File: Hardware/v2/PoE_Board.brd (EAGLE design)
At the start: 84.6 x 72.1 mm, 93 parts, among them U1 EDISON_CONNECTOR_FULLMOUNTING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, U2 LAN9512-JZX, U3 MAX4995AAUT+, U4 EDISON_CONNECTOR_FULLHEADER

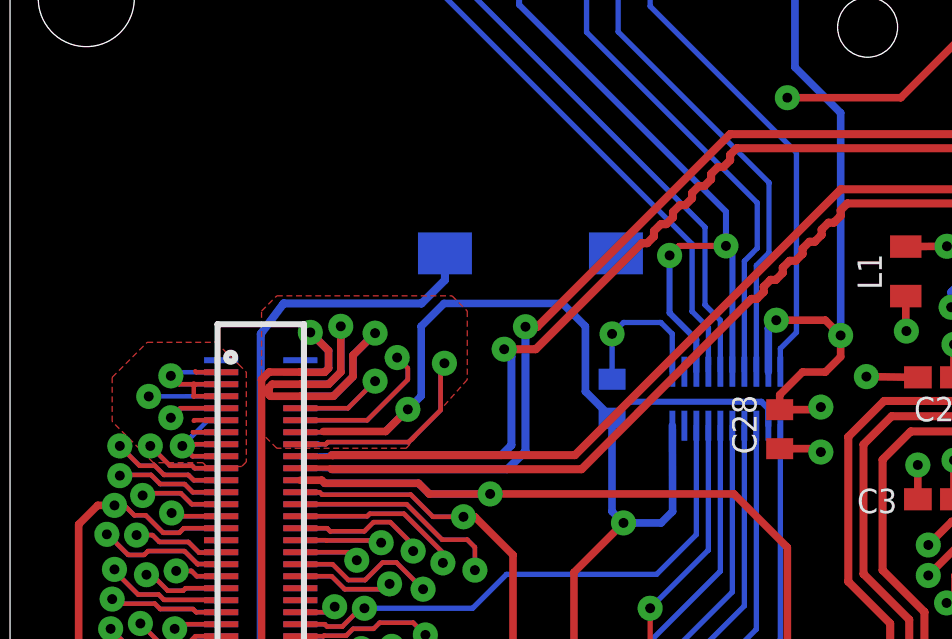
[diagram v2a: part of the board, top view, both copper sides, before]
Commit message: Connected shield pins on Ethernet jack
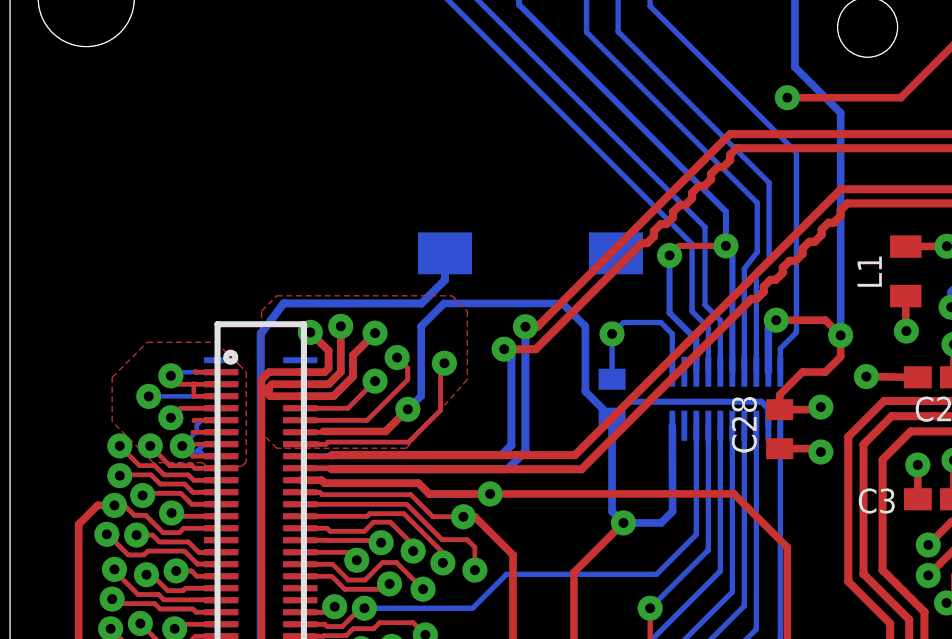
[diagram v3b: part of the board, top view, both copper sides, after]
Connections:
- net SHLD: now also X1.S1, X1.S2
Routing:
- net GND: track 147.3 -> 146.3 mm
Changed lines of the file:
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@@
 <grid distance="5" unitdist="mil" unit="mil" style="lines" multiple="1" display="yes" altdistance="0.25" altunitdist="mil" altunit="mil"/>
 <layers>
-<layer number="1" name="Top" color="4" fill="1" visible="no" active="yes"/>
+<layer number="1" name="Top" color="4" fill="1" visible="yes" active="yes"/>
 <layer number="2" name="gnd" color="11" fill="3" visible="yes" active="yes"/>
 <layer number="3" name="pwr" color="13" fill="3" visible="yes" active="yes"/>
@@
 <contactref element="U4" pad="13"/>
 <contactref element="U4" pad="15"/>
-<wire x1="5.7666" y1="49.1928" x2="5.327" y2="49.1928" width="0.1524" layer="16"/>
-<wire x1="5.327" y1="49.1928" x2="4.4704" y2="48.3362" width="0.1524" layer="16"/>
-<wire x1="5.7666" y1="48.7928" x2="4.927" y2="48.7928" width="0.1524" layer="16"/>
-<wire x1="4.927" y1="48.7928" x2="4.4704" y2="48.3362" width="0.1524" layer="16"/>
-<wire x1="5.7666" y1="48.3928" x2="4.527" y2="48.3928" width="0.1524" layer="16"/>
-<wire x1="4.527" y1="48.3928" x2="4.4704" y2="48.3362" width="0.1524" layer="16"/>
-<wire x1="5.7666" y1="47.9928" x2="4.8138" y2="47.9928" width="0.1524" layer="16"/>
-<wire x1="4.8138" y1="47.9928" x2="4.4704" y2="48.3362" width="0.1524" layer="16"/>
 <contactref element="U4" pad="5"/>
 <wire x1="5.7666" y1="49.9928" x2="3.3528" y2="49.9872" width="0.1524" layer="16"/>
+<wire x1="5.7666" y1="49.1928" x2="5.1238" y2="49.1928" width="0.1524" layer="16"/>
+<wire x1="5.1238" y1="49.1928" x2="4.953" y2="49.022" width="0.1524" layer="16"/>
+<wire x1="4.953" y1="49.022" x2="4.953" y2="48.8188" width="0.1524" layer="16"/>
+<wire x1="4.953" y1="48.8188" x2="4.4704" y2="48.3362" width="0.1524" layer="16"/>
+<wire x1="5.7666" y1="48.7928" x2="4.979" y2="48.7928" width="0.1524" layer="16"/>
+<wire x1="4.979" y1="48.7928" x2="4.953" y2="48.8188" width="0.1524" layer="16"/>
+<wire x1="5.7666" y1="48.3928" x2="5.2001" y2="48.3928" width="0.1524" layer="16"/>
+<wire x1="5.2001" y1="48.3928" x2="5.01015" y2="48.20285" width="0.1524" layer="16"/>
+<wire x1="5.01015" y1="48.20285" x2="4.95935" y2="48.15205" width="0.1524" layer="16"/>
+<wire x1="4.95935" y1="48.15205" x2="4.65455" y2="48.15205" width="0.1524" layer="16"/>
+<wire x1="4.65455" y1="48.15205" x2="4.4704" y2="48.3362" width="0.1524" layer="16"/>
+<wire x1="5.7666" y1="47.9928" x2="5.2202" y2="47.9928" width="0.1524" layer="16"/>
+<wire x1="5.2202" y1="47.9928" x2="5.01015" y2="48.20285" width="0.1524" layer="16"/>
 </signal>
 <signal name="N$1">
@@
 </polygon>
 <contactref element="R10" pad="1"/>
+<contactref element="X1" pad="S1"/>
+<contactref element="X1" pad="S2"/>
 </signal>
 <signal name="USBSHLD">
@@
 <contactref element="USD" pad="2"/>
 <contactref element="U6" pad="18"/>
-<wire x1="23.606" y1="50.811" x2="23.606" y2="54.3527" width="0.1778" layer="16"/>
-<wire x1="23.606" y1="54.3527" x2="24.0284" y2="54.7751" width="0.1778" layer="16"/>
-<wire x1="24.0284" y1="54.7751" x2="24.0284" y2="57.1119" width="0.1778" layer="16"/>
+<wire x1="23.606" y1="50.811" x2="23.606" y2="54.0987" width="0.1778" layer="16"/>
+<wire x1="23.606" y1="54.0987" x2="24.0284" y2="54.5211" width="0.1778" layer="16"/>
+<wire x1="24.0284" y1="54.5211" x2="24.0284" y2="57.1119" width="0.1778" layer="16"/>
 <wire x1="24.0284" y1="57.1119" x2="18.9992" y2="62.1411" width="0.1778" layer="16"/>
 <wire x1="18.9992" y1="62.1411" x2="18.9992" y2="64.436" width="0.1778" layer="16"/>
@@
 <contactref element="USD" pad="3"/>
 <contactref element="U6" pad="17"/>
-<wire x1="23.206" y1="50.811" x2="23.206" y2="54.4957" width="0.1778" layer="16"/>
-<wire x1="23.206" y1="54.4957" x2="23.6347" y2="54.9275" width="0.1778" layer="16"/>
-<wire x1="23.6347" y1="54.9275" x2="23.6347" y2="56.4388" width="0.1778" layer="16"/>
+<wire x1="23.206" y1="50.811" x2="23.206" y2="54.2417" width="0.1778" layer="16"/>
+<wire x1="23.206" y1="54.2417" x2="23.6347" y2="54.8005" width="0.1778" layer="16"/>
+<wire x1="23.6347" y1="54.8005" x2="23.6347" y2="56.4388" width="0.1778" layer="16"/>
 <wire x1="23.6347" y1="56.4388" x2="17.9451" y2="62.1284" width="0.1778" layer="16"/>
 <wire x1="17.9451" y1="62.1284" x2="17.9451" y2="64.7827" width="0.1778" layer="16"/>

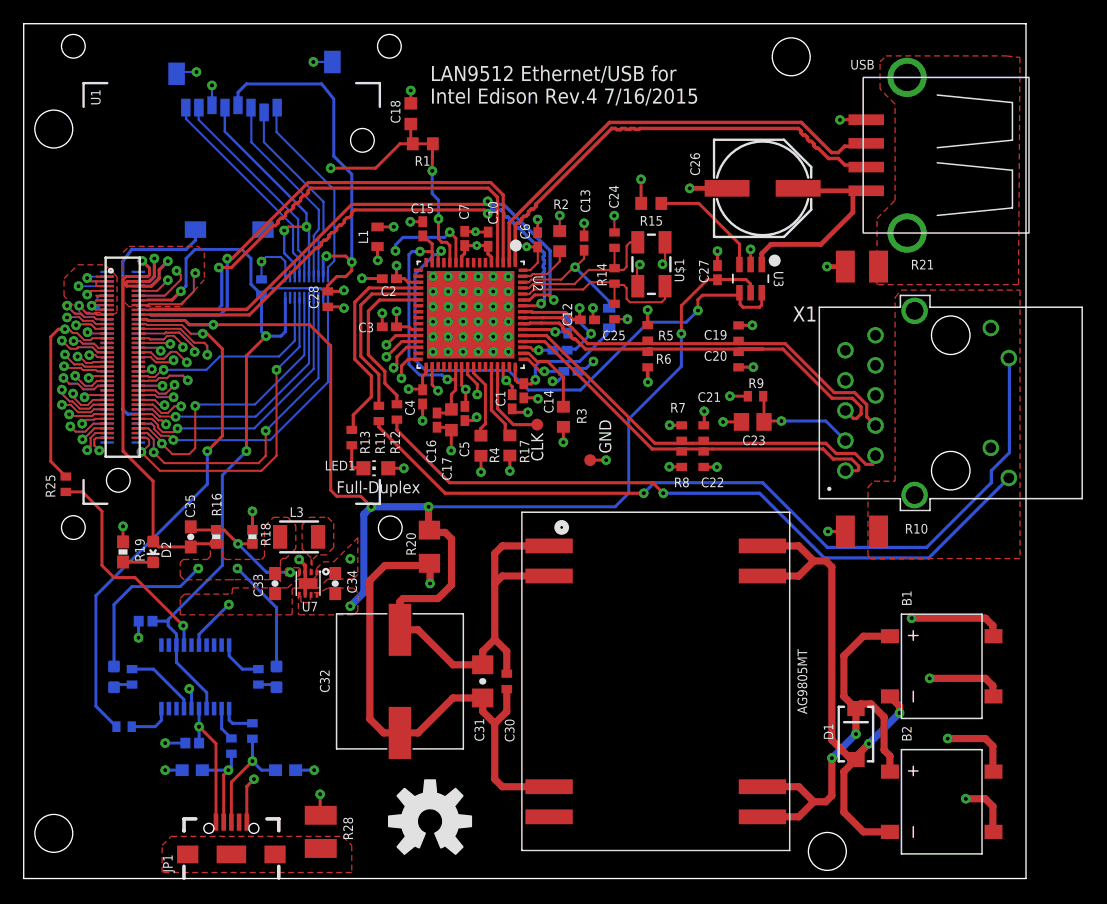
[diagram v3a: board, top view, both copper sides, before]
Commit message: Moved U8 to top of board, moved LED1 from under the Edison, put C28 back on the bottom
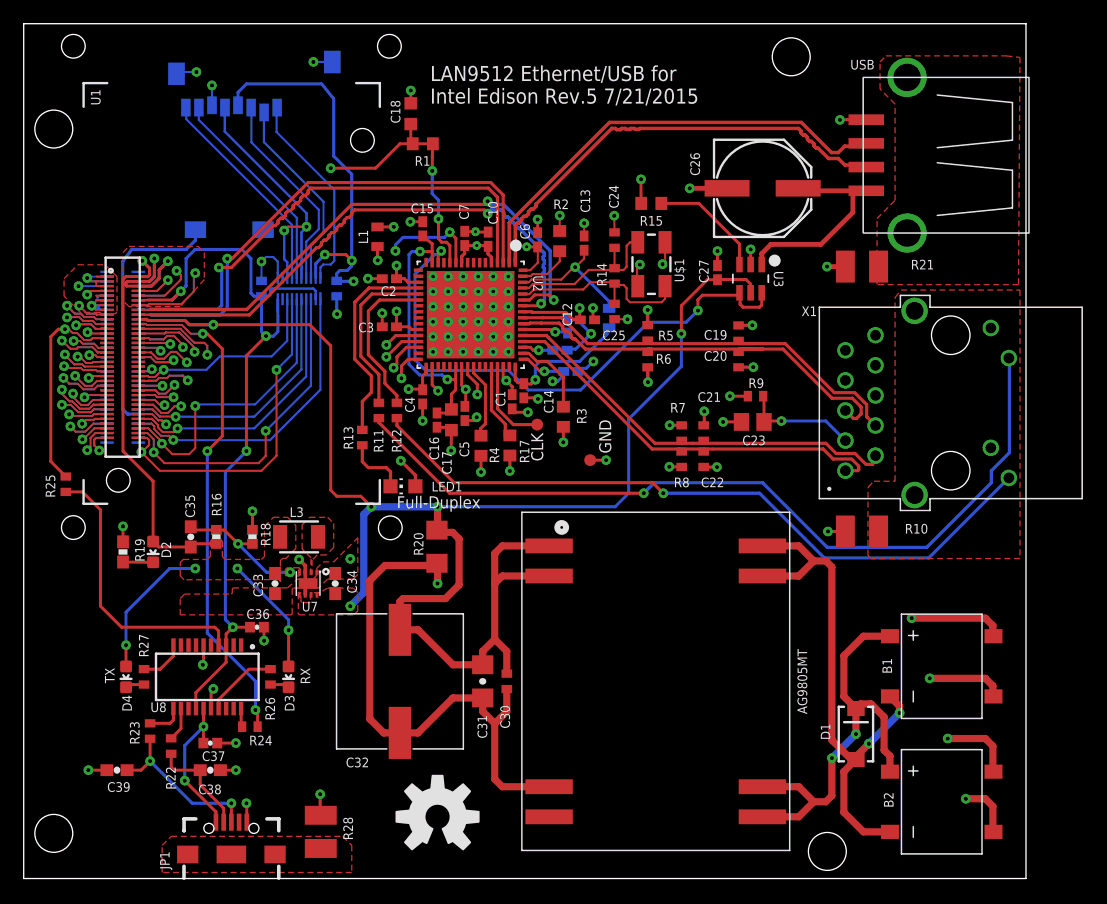
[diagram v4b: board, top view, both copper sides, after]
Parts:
- moved D3 14.7 mm to (21.1, 17.0), flipped to the top
- moved C39 14.2 mm to (6.60, 9.14), flipped to the top
- moved D4 12.7 mm to (7.37, 17.0), flipped to the top
- moved R26 11.7 mm to (19.6, 17.0), flipped to the top
- moved R24 10.6 mm to (17.8, 12.8), flipped to the top
- moved R27 9.65 mm to (8.89, 17.0), flipped to the top
- moved C36 9.41 mm to (18.4, 21.2), flipped to the top
- moved R23 8.64 mm to (9.40, 12.4), flipped to the top
- moved R22 5.08 mm to (11.2, 11.2), flipped to the top
- moved LED1 2.75 mm to (30.7, 33.1)
- moved C37 1.52 mm to (14.5, 11.4), flipped to the top
- moved C38 1.52 mm to (14.5, 9.14), flipped to the top
- moved C28 1.17 mm to (25.1, 49.8), flipped to the bottom
- moved U8 1.02 mm to (14.2, 17.0), flipped to the top
- moved R13 0.89 mm to (27.3, 37.2)
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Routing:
- net GND: track 146.3 -> 139.2 mm
- net S$22: track 18.9 -> 23.7 mm, vias 1 -> 0
- net S$17: track 10.0 -> 14.1 mm, vias 1 -> 2
- net P22: track 50.8 -> 47.9 mm, vias 2 -> 3
- net N$19: track 2.82 -> 5.34 mm
- net 2_VCCA_1V8: track 72.2 -> 69.9 mm, vias 3 -> 4
- net S$23: track 3.71 -> 1.56 mm
- net VDD3IO: track 147.6 -> 149.0 mm
- net VSYS: track 87.9 -> 86.7 mm, vias 6 -> 8
- net VBUS1: track 12.0 -> 13.2 mm, vias 1 -> 2
- net 8_A7_SDCLKFB: track 20.8 -> 20.1 mm
- net 20_B1_NC: track 16.5 -> 17.3 mm
- net S$15: track 8.24 -> 8.89 mm, vias 1 -> 0
- net S$5: track 44.2 -> 44.8 mm
- net USB_VBUS: track 144.0 -> 144.6 mm
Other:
- board text added: "LAN9512 Ethernet/USB for Intel Edison Rev.5 7/21/2015"
- board text removed: "LAN9512 Ethernet/USB for Intel Edison Rev.4 7/16/2015"

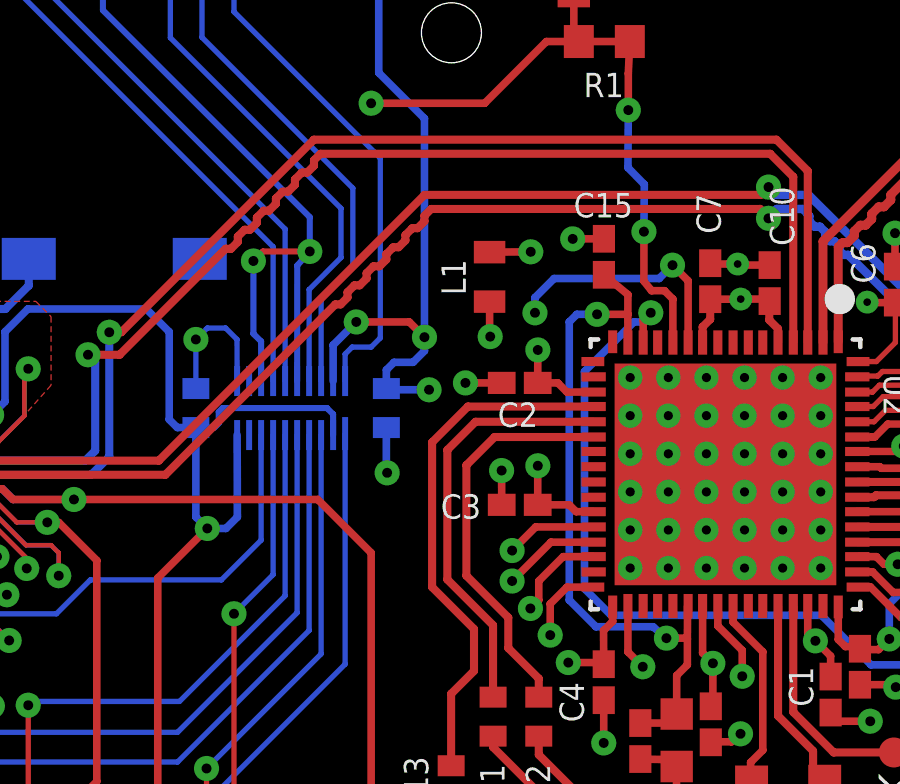
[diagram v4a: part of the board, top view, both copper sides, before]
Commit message: Minor changes in via placement
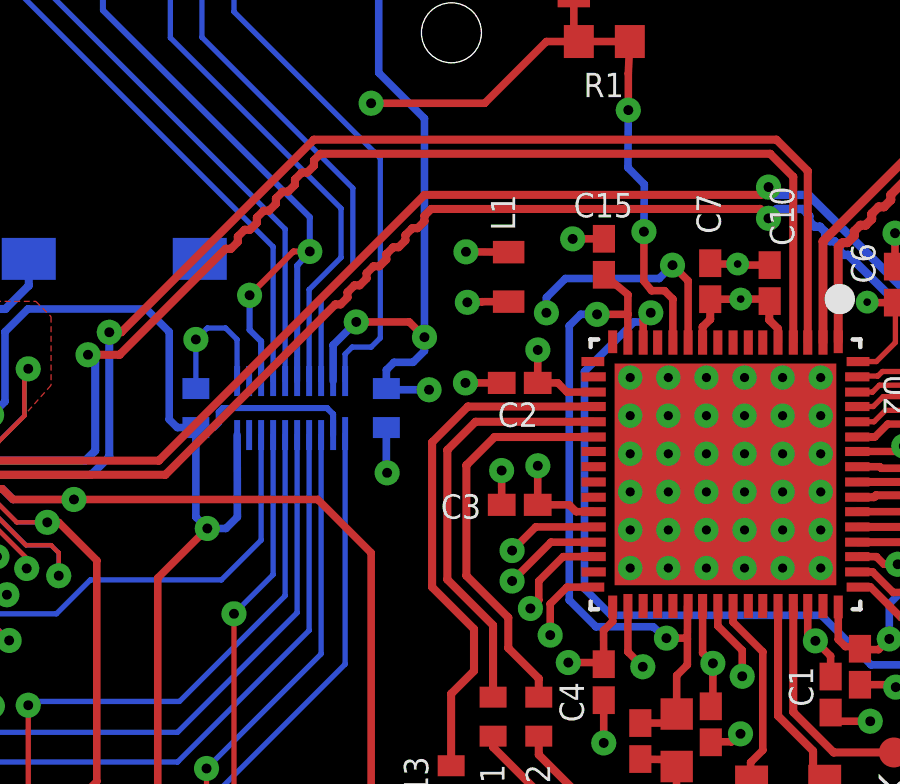
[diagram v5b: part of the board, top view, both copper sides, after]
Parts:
- moved L1 0.64 mm to (29.2, 54.2)
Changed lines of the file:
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@@
 <attribute name="NAME" x="70.541" y="69.0848" size="0.8128" layer="25" ratio="15" rot="R180"/>
 </element>
-<element name="L1" library="murata-inductors" package="L0603" value="2.0A 120Ohm" x="28.587" y="54.1562" smashed="yes" rot="R90">
-<attribute name="NAME" x="27.792" y="53.5442" size="0.8128" layer="25" ratio="15" rot="R90"/>
+<element name="L1" library="murata-inductors" package="L0603" value="2.0A 120Ohm" x="29.222" y="54.1562" smashed="yes" rot="R90">
+<attribute name="NAME" x="29.443" y="55.7032" size="0.8128" layer="25" ratio="15" rot="R90"/>
 </element>
 <element name="L2" library="murata-inductors" package="L0603" value="2.0A 120Ohm" x="48.133" y="47.2948" smashed="yes" rot="MR270">
@@
 <via x="42.1894" y="44.577" extent="1-16" drill="0.3302"/>
 <wire x1="40.844" y1="44.8302" x2="40.8432" y2="44.831" width="0.1524" layer="1"/>
-<wire x1="28.587" y1="54.9812" x2="29.9586" y2="54.9918" width="0.254" layer="1"/>
-<via x="29.9586" y="54.9918" extent="1-16" drill="0.3302"/>
+<wire x1="29.222" y1="54.9812" x2="27.7996" y2="54.9918" width="0.254" layer="1"/>
+<via x="27.7996" y="54.9918" extent="1-16" drill="0.3302"/>
 <via x="42.672" y="42.799" extent="1-16" drill="0.3302"/>
 <wire x1="40.894" y1="43.7642" x2="40.8686" y2="43.815" width="0.1524" layer="1"/>
@@
 <wire x1="33.195259375" y1="52.9082" x2="32.1691" y2="52.9082" width="0.254" layer="1"/>
 <via x="32.1691" y="52.9082" extent="1-16" drill="0.3302"/>
-<wire x1="32.1691" y1="52.9082" x2="31.496" y2="52.9082" width="0.254" layer="16"/>
-<wire x1="31.496" y1="52.9082" x2="31.242" y2="52.6542" width="0.254" layer="16"/>
-<wire x1="31.242" y1="52.6542" x2="31.242" y2="43.3832" width="0.254" layer="16"/>
+<wire x1="32.1691" y1="52.9082" x2="31.623" y2="52.9082" width="0.254" layer="16"/>
+<wire x1="31.623" y1="52.9082" x2="31.242" y2="52.5272" width="0.254" layer="16"/>
+<wire x1="31.242" y1="52.5272" x2="31.242" y2="43.3832" width="0.254" layer="16"/>
 <wire x1="31.242" y1="43.3832" x2="32.131" y2="42.4942" width="0.254" layer="16"/>
 <wire x1="32.131" y1="42.4942" x2="34.036" y2="42.4942" width="0.254" layer="16"/>
@@
 <wire x1="15.6972" y1="65.0372" x2="15.716" y2="65.056" width="0.2032" layer="16"/>
 <wire x1="20.971" y1="50.684" x2="20.971" y2="52.0065" width="0.2032" layer="16"/>
-<wire x1="20.971" y1="52.0065" x2="20.7137" y2="52.2605" width="0.2032" layer="16"/>
-<wire x1="20.7137" y1="52.2605" x2="20.7137" y2="54.6862" width="0.2032" layer="16"/>
-<wire x1="20.7137" y1="54.6862" x2="21.0312" y2="55.0037" width="0.2032" layer="1"/>
-<via x="20.7137" y="54.6862" extent="1-16" drill="0.3302"/>
+<wire x1="20.971" y1="52.0065" x2="20.5867" y2="52.3875" width="0.2032" layer="16"/>
+<wire x1="20.5867" y1="52.3875" x2="20.5867" y2="53.5432" width="0.2032" layer="16"/>
+<wire x1="20.5867" y1="53.5432" x2="22.0472" y2="55.0037" width="0.2032" layer="1"/>
+<via x="20.5867" y="53.5432" extent="1-16" drill="0.3302"/>
 <via x="22.5933" y="55.0037" extent="1-16" drill="0.3302"/>
-<wire x1="21.0312" y1="55.0037" x2="22.5933" y2="55.0037" width="0.2032" layer="1"/>
+<wire x1="22.0472" y1="55.0037" x2="22.5933" y2="55.0037" width="0.2032" layer="1"/>
 <wire x1="22.5933" y1="56.1467" x2="22.5933" y2="55.0037" width="0.2032" layer="16"/>
 </signal>
@@
 <wire x1="30.191" y1="50.6222" x2="30.191" y2="50.81595" width="0.254" layer="1"/>
 <wire x1="30.861" y1="50.6222" x2="30.191" y2="50.6222" width="0.254" layer="1"/>
-<via x="30.099" y="52.959" extent="1-16" drill="0.3302"/>
+<via x="30.48" y="52.959" extent="1-16" drill="0.3302"/>
 <via x="34.6837" y="54.5465" extent="1-16" drill="0.3302"/>
-<wire x1="30.099" y1="52.959" x2="30.099" y2="53.467" width="0.254" layer="16"/>
-<wire x1="30.099" y1="53.467" x2="30.734" y2="54.102" width="0.254" layer="16"/>
-<wire x1="30.734" y1="54.102" x2="34.2392" y2="54.102" width="0.254" layer="16"/>
+<wire x1="30.48" y1="52.959" x2="30.48" y2="53.467" width="0.254" layer="16"/>
+<wire x1="30.48" y1="53.467" x2="31.115" y2="54.102" width="0.254" layer="16"/>
+<wire x1="31.115" y1="54.102" x2="34.2392" y2="54.102" width="0.254" layer="16"/>
 <wire x1="34.2392" y1="54.102" x2="34.6837" y2="54.5465" width="0.254" layer="16"/>
 <contactref element="U2" pad="11"/>
 <wire x1="35.2044" y1="51.9684" x2="35.2044" y2="54.0258" width="0.254" layer="1"/>
 <wire x1="35.2044" y1="54.0258" x2="34.6837" y2="54.5465" width="0.254" layer="1"/>
-<via x="28.60675" y="52.16525" extent="1-16" drill="0.3302"/>
+<via x="27.84475" y="53.30825" extent="1-16" drill="0.3302"/>
 <contactref element="L1" pad="1"/>
-<wire x1="28.587" y1="53.3312" x2="28.587" y2="52.185" width="0.254" layer="1"/>
-<wire x1="28.587" y1="52.185" x2="28.60675" y2="52.16525" width="0.254" layer="1"/>
+<wire x1="29.222" y1="53.3312" x2="28.333" y2="53.328" width="0.254" layer="1"/>
+<wire x1="28.333" y1="53.328" x2="27.84475" y2="53.30825" width="0.254" layer="1"/>
 <contactref element="U1" pad="8"/>
 <wire x1="9.9942" y1="49.5928" x2="10.8966" y2="50.4952" width="0.1524" layer="16"/>
